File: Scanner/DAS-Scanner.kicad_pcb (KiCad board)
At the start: 2 copper layers, 24 x 62.8 mm, 33 parts, among them J1 TETST_PORT, J2 ANT, J3 LOG_PORT, J4 PWR_PORT, P1 USB_C_Plug_USB2.0, P2 USB_C_Plug_USB2.0, SW1 SW_Push, U1 CH585M, U2 ME6210A33M3G, Y1 32.768kHz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

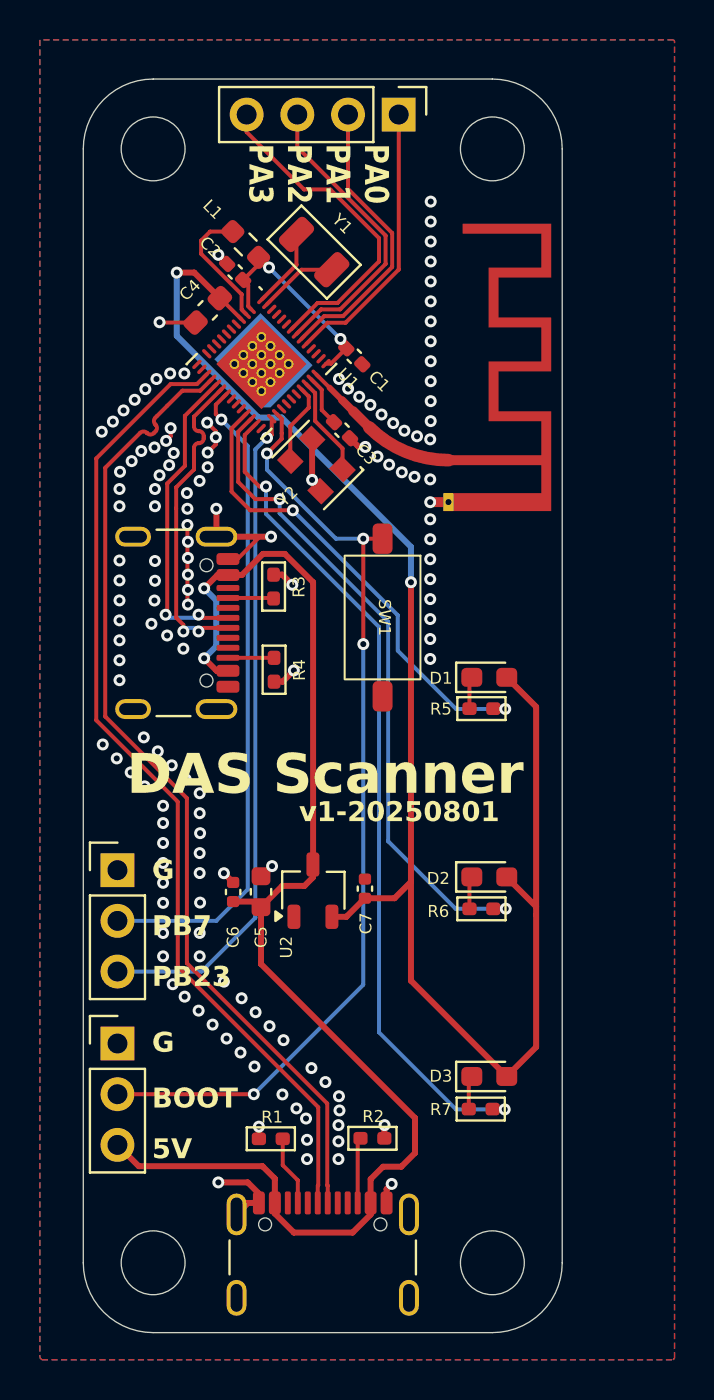
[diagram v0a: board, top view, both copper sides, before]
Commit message: opt ANT ground and M3 hole
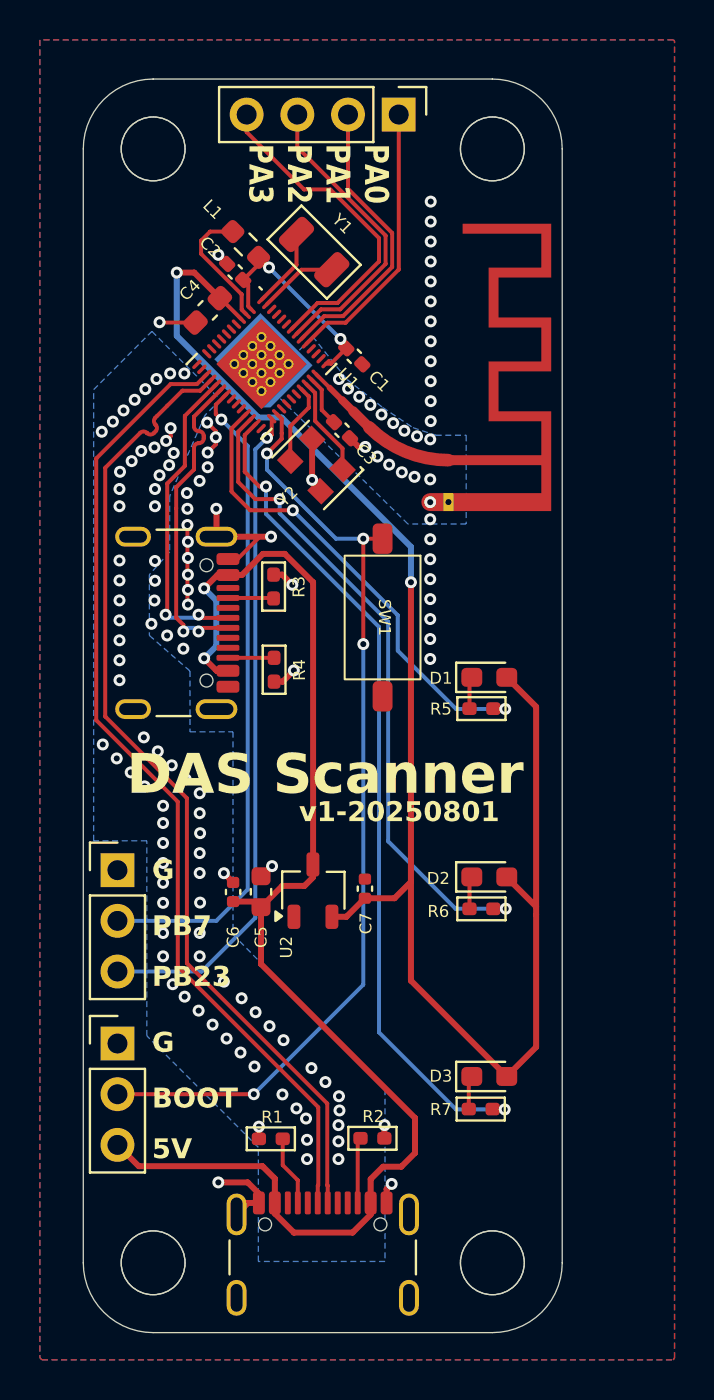
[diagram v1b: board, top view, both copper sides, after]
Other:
- outline, holes or cut-outs redrawn
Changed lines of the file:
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@@
 		(tenting front back)
 		(pcbplotparams
-			(layerselection 0x00000000_00000000_55555555_5755f5ff)
+			(layerselection 0x00000000_00000000_5555555f_5755f5ff)
 			(plot_on_all_layers_selection 0x00000000_00000000_00000000_00000000)
 			(disableapertmacros no)
@@
 			(outputformat 1)
 			(mirror no)
-			(drillshape 1)
+			(drillshape 0)
 			(scaleselection 1)
-			(outputdirectory "")
+			(outputdirectory "output")
 		)
 	)
@@
 			(pintype "input")
 			(thermal_bridge_angle 45)
+			(teardrops
+				(best_length_ratio 0.5)
+				(max_length 1)
+				(best_width_ratio 1)
+				(max_width 2)
+				(curved_edges yes)
+				(filter_ratio 0.9)
+				(enabled yes)
+				(allow_two_segments yes)
+				(prefer_zone_connections yes)
+			)
 		)
 		(pad "35" smd oval
@@
 			(pinfunction "Pin_1")
 			(pintype "passive")
+			(teardrops
+				(best_length_ratio 0.5)
+				(max_length 1)
+				(best_width_ratio 1)
+				(max_width 2)
+				(curved_edges yes)
+				(filter_ratio 0.9)
+				(enabled yes)
+				(allow_two_segments yes)
+				(prefer_zone_connections yes)
+			)
 		)
 		(pad "2" thru_hole rect
@@
 		(layer "Edge.Cuts")
 	)
+	(gr_circle
+		(center 108.5 63.5)
+		(end 110.1 63.5)
+		(stroke
+			(width 0.05)
+			(type default)
+		)
+		(fill no)
+		(layer "Edge.Cuts")
+	)
 	(gr_line
 		(start 112 63.5)
@@
 		(layer "Edge.Cuts")
 	)
+	(gr_circle
+		(center 108.5 119.3181)
+		(end 110.1 119.3181)
+		(stroke
+			(width 0.05)
+			(type default)
+		)
+		(fill no)
+		(layer "Edge.Cuts")
+	)
+	(gr_circle
+		(center 91.5 119.3181)
+		(end 93.1 119.3181)
+		(stroke
+			(width 0.05)
+			(type default)
+		)
+		(fill no)
+		(layer "Edge.Cuts")
+	)
 	(gr_line
 		(start 108.499983 59.999983)
@@
 		(layer "Edge.Cuts")
 	)
+	(gr_circle
+		(center 91.5 63.5)
+		(end 93.1 63.5)
+		(stroke
+			(width 0.05)
+			(type default)
+		)
+		(fill no)
+		(layer "Edge.Cuts")
+	)
 	(gr_text "G"
 		(at 91.44 107.696 0)
@@
 		(start 106.299 81.199)
 		(end 105.3894 81.199)
-		(width 0.5)
+		(width 0.9)
 		(layer "F.Cu")
 		(net 1)
@@
 			)
 		)
+	)
+	(zone
+		(net 1)
+		(net_name "GND")
+		(layer "B.Cu")
+		(name "GND")
+		(hatch edge 0.5)
+		(priority 1)
+		(connect_pads
+			(clearance 0.35)
+		)
+		(min_thickness 0.25)
+		(filled_areas_thickness no)
+		(fill yes
+			(thermal_gap 0.5)
+			(thermal_bridge_width 0.5)
+			(smoothing fillet)
+		)
+		(polygon
+			(pts
+				(xy 99.4918 72.898) (xy 101.219 75.057) (xy 102.997 76.454) (xy 104.521 77.47) (xy 105.664 77.851)
+				(xy 107.188 77.851) (xy 107.188 82.296) (xy 104.267 82.296) (xy 97.155 75.311)
+			)
+		)
+	)
+	(zone
+		(net 1)
+		(net_name "GND")
+		(layer "B.Cu")
+		(name "GND")
+		(hatch edge 0.5)
+		(priority 2)
+		(connect_pads
+			(clearance 0.35)
+		)
+		(min_thickness 0.25)
+		(filled_areas_thickness no)
+		(fill yes
+			(thermal_gap 0.5)
+			(thermal_bridge_width 0.5)
+			(smoothing fillet)
+		)
+		(polygon
+			(pts
+				(xy 94.869 76.073) (xy 94.107 76.835) (xy 92.329 80.899) (xy 92.329 83.693) (xy 91.313 84.836) (xy 91.313 87.884)
+				(xy 93.345 89.662) (xy 93.345 92.71) (xy 95.504 92.71) (xy 95.504 102.87) (xy 103.124 110.617) (xy 103.124 119.253)
+				(xy 96.774 119.253) (xy 96.774 113.538) (xy 91.186 107.95) (xy 91.186 98.171) (xy 88.519 98.171)
+				(xy 88.519 75.565) (xy 91.44 72.644)
+			)
+		)
